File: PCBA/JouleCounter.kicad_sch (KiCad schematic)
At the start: 2 parts, among them J101 JTAG, J102 Qwiic

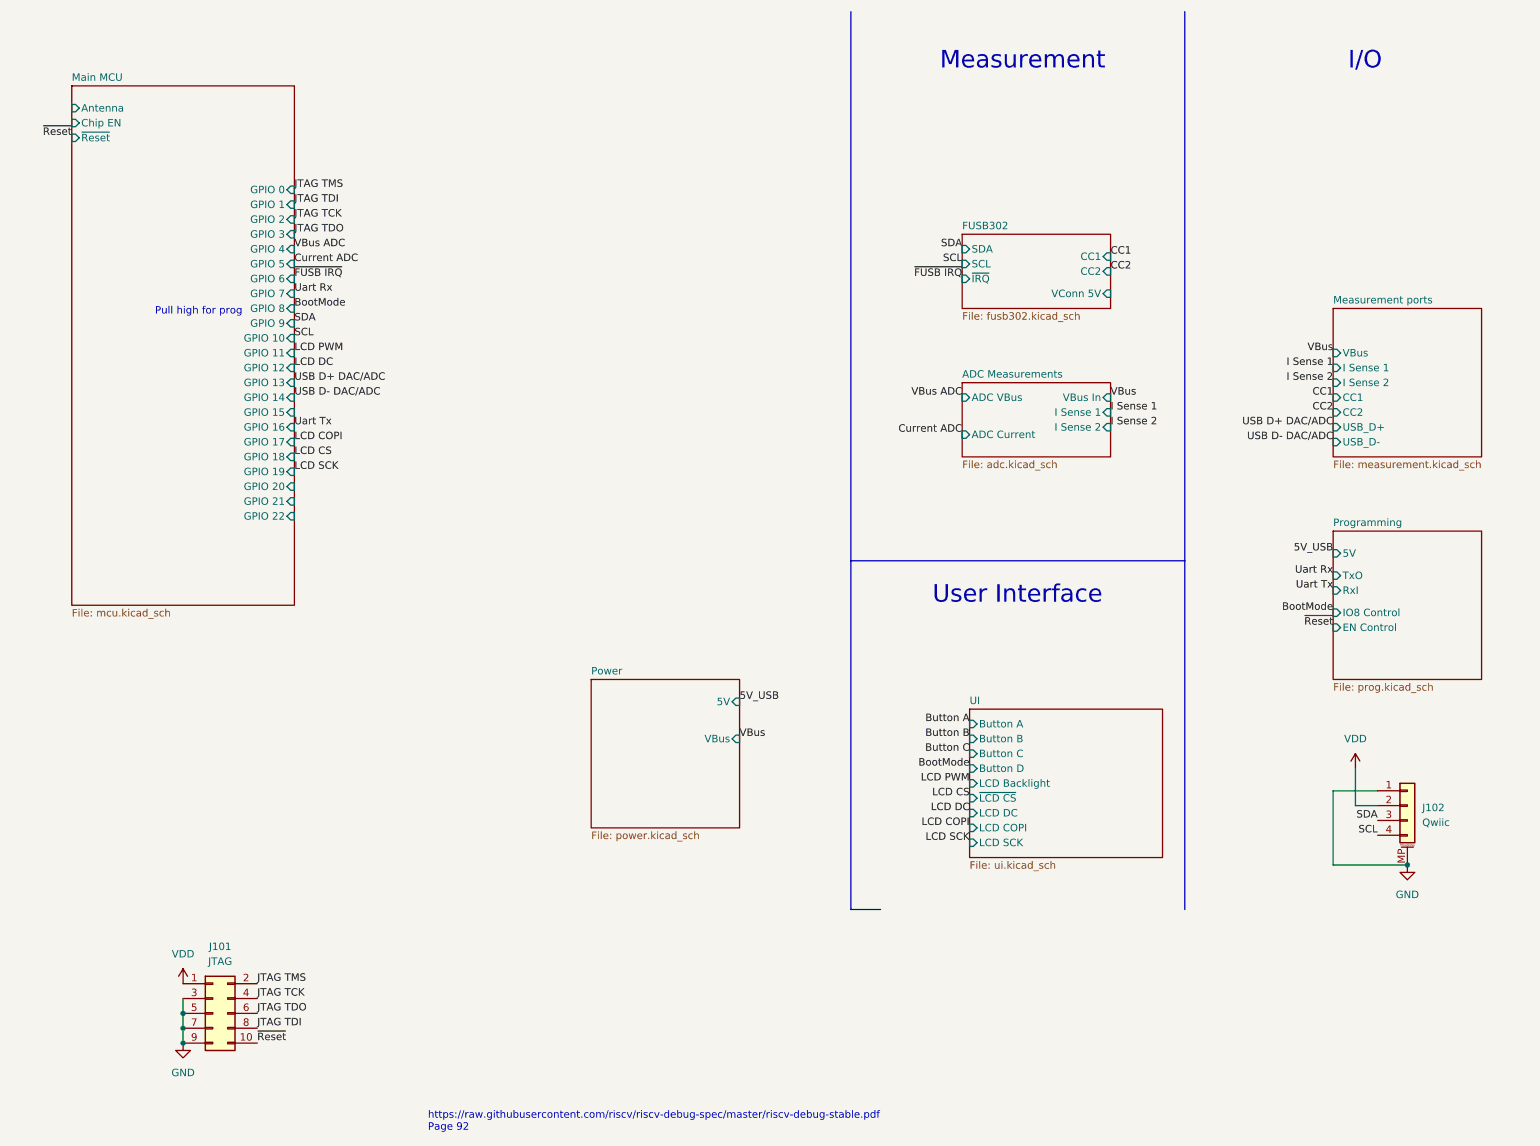
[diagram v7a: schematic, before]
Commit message: Update schematic pinmap bl706
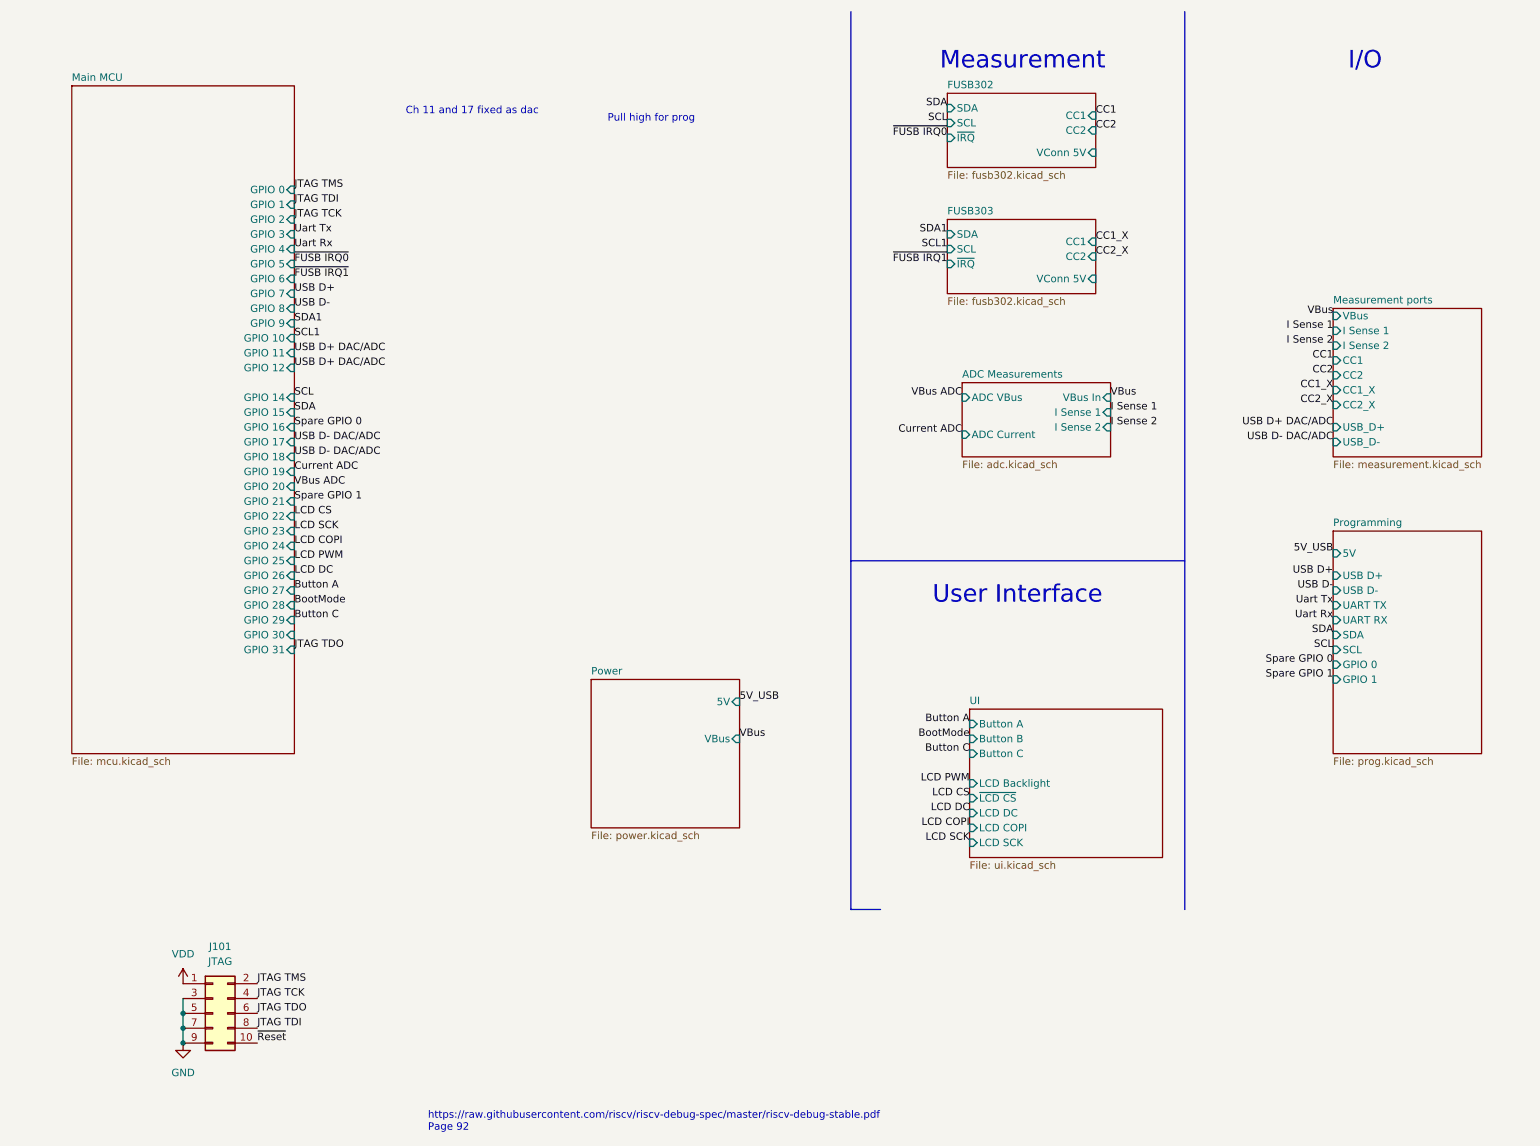
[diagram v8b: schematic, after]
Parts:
- removed J102: Qwiic, Connector_JST:JST_SH_BM04B-SRSS-TB_1x04-1MP_P1.00mm_Vertical, symbol Connector_Generic_MountingPin:Conn_01x04_MountingPin
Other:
- added sheet FUSB303 (fusb302.kicad_sch)
- sheet Main MCU ports: added GPIO 23, GPIO 24, GPIO 25, GPIO 26, GPIO 27, GPIO 28, GPIO 29, GPIO 30, GPIO 31; removed Antenna, Chip EN, GPIO 13, ~{Reset}
- sheet Measurement ports ports: added CC1_X, CC2_X; removed none
- sheet Programming ports: added GPIO 0, GPIO 1, SCL, SDA, UART RX, UART TX, USB D+, USB D-; removed EN Control, IO8 Control, RxI, TxO
- sheet UI ports: added none; removed Button D
- note added: "Ch 11 and 17 fixed as dac"
